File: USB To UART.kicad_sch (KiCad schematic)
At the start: 5 parts, among them U1 USB_to_COM_QFN-20_FT231XQ

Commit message: Finished capturing schematics
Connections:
- net at D2.1 (K): now also U1.14 (CBUS1); no longer U1.7 (CBUS2)
- net at D2.2 (A): now also R1.2; no longer R2.2
- net at D1.2 (A): now also R2.2; no longer R1.2
- net at D1.1 (K): now also U1.7 (CBUS2); no longer U1.14 (CBUS1)
- net GPIO: now reaches U1.16 (CBUS3)
- net GND renamed GND USB
- no-connect marks 7 -> 6

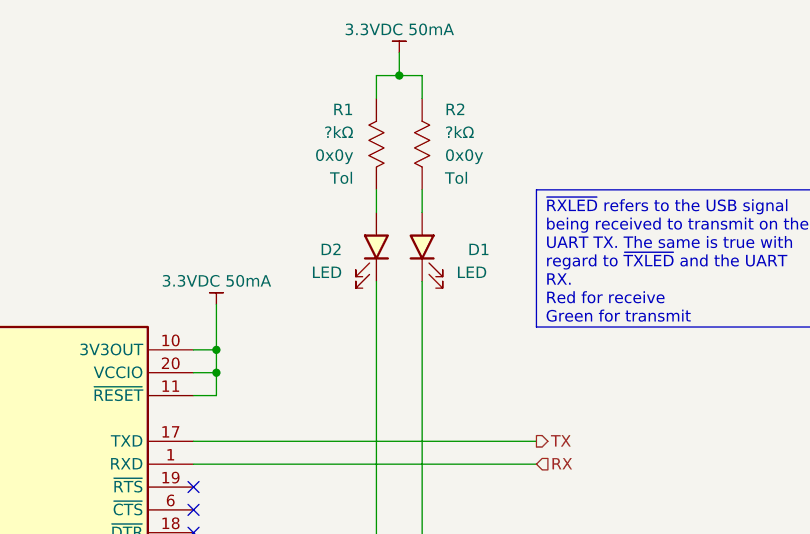
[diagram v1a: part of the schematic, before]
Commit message: Power & Level Translation
Isolated 5VDC changed and a 3.3VDC LDO was added. The original 5VDC was too expensive and big. The new one is still both, but less so.
The level translator is now a dedicated IC instead of MOSFETs. I was having trouble making it work the way I wanted.
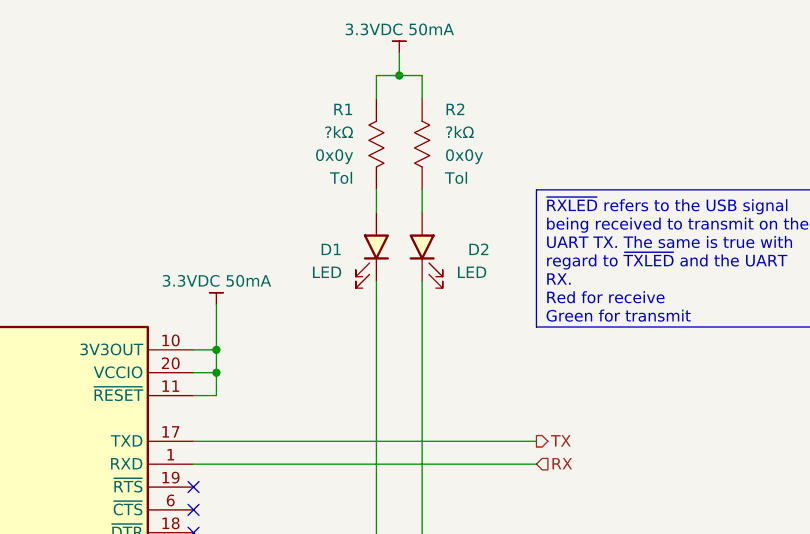
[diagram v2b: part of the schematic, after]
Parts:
- renumbered D2 to D1, D1 to D2
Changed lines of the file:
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@@
 		(dnp no)
 		(fields_autoplaced yes)
-		(property "Reference" "#PWR06"
+		(property "Reference" "#PWR09"
 			(at 124.46 82.55 0)
 			(effects
@@
 			(project "Isolated Com Port"
 				(path "/736fe05f-3e80-4c58-a4b9-c0a7b5ae4e97/20c906b9-666a-4d7a-8032-5080b03787b8"
-					(reference "#PWR06")
+					(reference "#PWR09")
 					(unit 1)
 				)
@@
 		(dnp no)
 		(fields_autoplaced yes)
-		(property "Reference" "#PWR08"
+		(property "Reference" "#PWR012"
 			(at 185.42 54.61 0)
 			(effects
@@
 			(project "Isolated Com Port"
 				(path "/736fe05f-3e80-4c58-a4b9-c0a7b5ae4e97/20c906b9-666a-4d7a-8032-5080b03787b8"
-					(reference "#PWR08")
+					(reference "#PWR012")
 					(unit 1)
 				)
@@
 		(dnp no)
 		(fields_autoplaced yes)
-		(property "Reference" "#PWR05"
+		(property "Reference" "#PWR010"
 			(at 124.46 135.89 0)
 			(effects
@@
 			(project "Isolated Com Port"
 				(path "/736fe05f-3e80-4c58-a4b9-c0a7b5ae4e97/20c906b9-666a-4d7a-8032-5080b03787b8"
-					(reference "#PWR05")
+					(reference "#PWR010")
 					(unit 1)
 				)
@@
 		(dnp no)
 		(fields_autoplaced yes)
-		(property "Reference" "#PWR07"
+		(property "Reference" "#PWR011"
 			(at 165.1 82.55 0)
 			(effects
@@
 			(project "Isolated Com Port"
 				(path "/736fe05f-3e80-4c58-a4b9-c0a7b5ae4e97/20c906b9-666a-4d7a-8032-5080b03787b8"
-					(reference "#PWR07")
+					(reference "#PWR011")
 					(unit 1)
 				)
@@
 		(on_board yes)
 		(dnp no)
-		(property "Reference" "D2"
+		(property "Reference" "D1"
 			(at 179.07 72.7074 90)
 			(effects
@@
 			(project "Isolated Com Port"
 				(path "/736fe05f-3e80-4c58-a4b9-c0a7b5ae4e97/20c906b9-666a-4d7a-8032-5080b03787b8"
-					(reference "D2")
+					(reference "D1")
 					(unit 1)
 				)
@@
 		(on_board yes)
 		(dnp no)
-		(property "Reference" "D1"
+		(property "Reference" "D2"
 			(at 193.04 72.7074 90)
 			(effects
@@
 			(project "Isolated Com Port"
 				(path "/736fe05f-3e80-4c58-a4b9-c0a7b5ae4e97/20c906b9-666a-4d7a-8032-5080b03787b8"
-					(reference "D1")
-					(unit 1)
-				)
+					(reference "D2")
+					(unit 1)
+				)

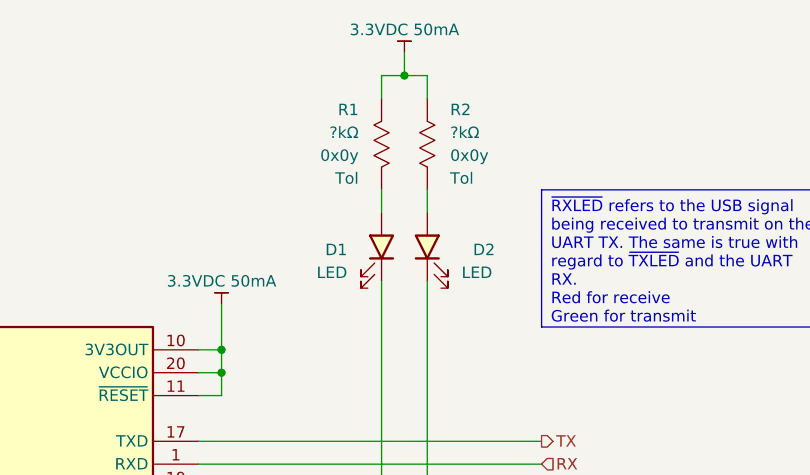
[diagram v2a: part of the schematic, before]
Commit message: RX/TX LEDs and resistors now reference actual parts
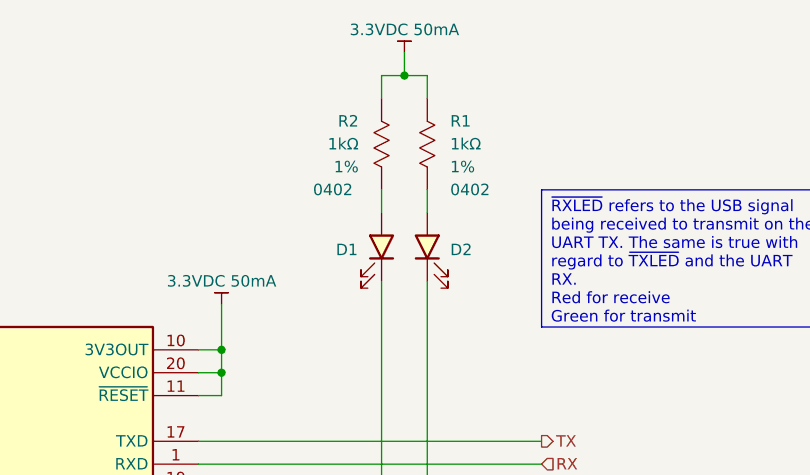
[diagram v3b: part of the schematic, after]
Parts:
- removed D1: LED, symbol Prototype Schematic Symbols - Isolated ComPort:Green_LED
- removed D2: LED, symbol Device:LED
- removed R1, R2: [Resistance] [Footprint] [Tolerance], symbol Prototype Schematic Symbols - Isolated ComPort:Resistor_Template
- added D1: LED, LED_SMD:LED_0402_1005Metric, symbol Prototype Schematic Symbols - Isolated ComPort:LED Green (570nm) 2.1V 20mA 0402
- added D2: LED, LED_SMD:LED_0402_1005Metric, symbol Prototype Schematic Symbols - Isolated ComPort:Red LED (630nm) 1.95V 20mA 0402
- added R1, R2: [Resistance] [Footprint] [Tolerance], Resistor_SMD:R_0402_1005Metric, symbol Prototype Schematic Symbols - Isolated ComPort:Resistor 1k 0402 1%
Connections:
- net 3.3VDC 50mA: now also R1.1, R2.1
- net at U1.14 (CBUS1): now also D1.1 (K)
- net at U1.7 (CBUS2): now also D2.1 (K)
- new net: D2.2 (A), R1.2
- new net: D1.2 (A), R2.2
